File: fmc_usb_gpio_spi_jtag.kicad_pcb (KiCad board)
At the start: 4 copper layers, 76.5 x 69 mm, 146 parts, among them J1 SAMTEC_ASP-134604-01, J2 ACA-SPI-004-K02, J3 USB_C_Receptacle, J4 USB_C_Receptacle, J5 Conn_JTAG_20, J6 PM2.54-2x6, J7 Micro_SD_Card_Det2, J8 PM2.54-2x6, SW1 DSHP04TSGET, SW10 TL3342F160QG, SW2 TL3342F160QG, SW7 TL3342F160QG, SW8 TL3342F160QG, SW9 TL3342F160QG, U1 M24C02-FMN, U11 TXS02612RTWR, U12 TPD4E02B04DQA, U13 MT2492, U14 TXS02612RTWR, U15 TXS02612RTWR, U16 TXS02612RTWR, U17 TXS02612RTWR, U18 TPD4E02B04DQA, U19 TPD4E02B04DQA, U2 STUSB03EQR, U20 TPD4E02B04DQA, U21 AIP74LVC1T45GB236TR, U22 AIP74LVC1T45GB236TR, U23 AIP74LVC1T45GB236TR, U24 AIP74LVC1T45GB236TR, U25 MMC5603NJ, U26 TXS02612RTWR, U27 TXS02612RTWR, U3 CP2104, U4 TXS02612RTWR, U5 GX0011D

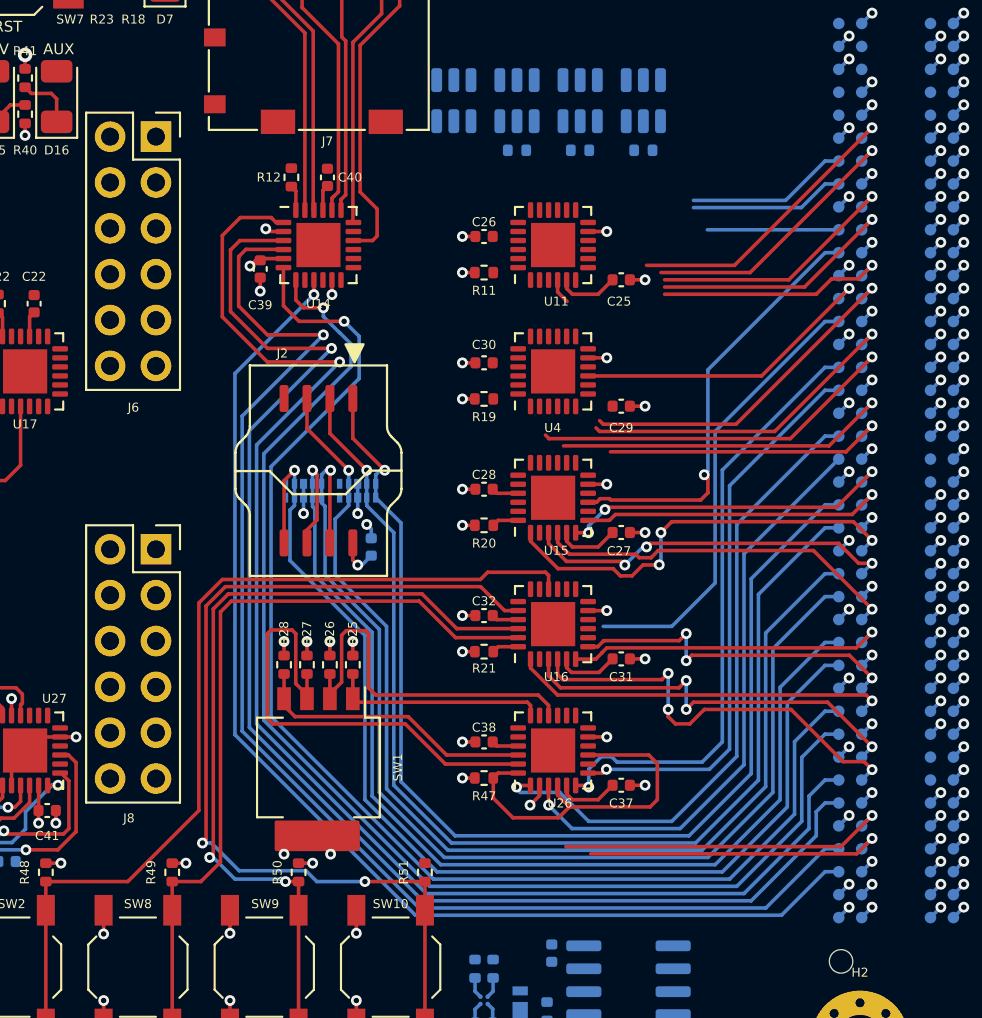
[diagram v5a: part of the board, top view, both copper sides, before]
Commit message: *.kicad_pcb: finish layout of U4, U11
Signed-off-by: Huang Rui <vowstar@gmail.com>
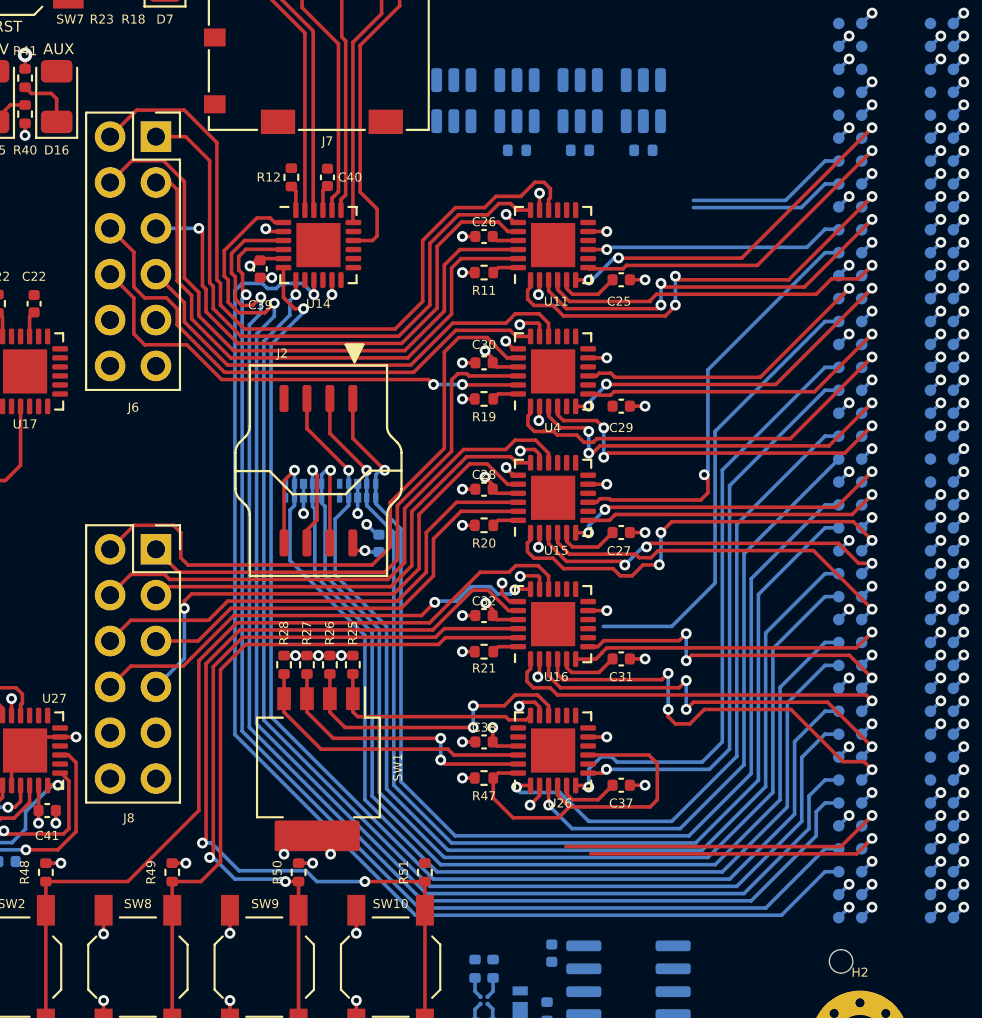
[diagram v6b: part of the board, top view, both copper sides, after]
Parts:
- moved C5 0.47 mm to (87.7, 100.5)
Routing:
- net /GPIO/HVGPIO1: track 0.00 -> 41.9 mm
- net /GPIO/HVGPIO0: track 0.00 -> 35.2 mm
- net /GPIO/HVGPIO3: track 0.00 -> 35.2 mm
- net /GPIO/HVGPIO9: track 0.00 -> 35.2 mm
- net /GPIO/HVGPIO2: track 0.00 -> 31.6 mm
- net /GPIO/HVGPIO11: track 0.00 -> 30.7 mm
- net /GPIO/HVGPIO4: track 0.00 -> 30.2 mm, vias 0 -> 1
- net /GPIO/HVGPIO5: track 0.00 -> 29.4 mm
- net /GPIO/HVGPIO8: track 0.00 -> 29.3 mm
- net /GPIO/HVGPIO14: track 0.00 -> 29.3 mm, vias 0 -> 1
- net /GPIO/HVGPIO13: track 0.00 -> 27.1 mm
- net /GPIO/HVGPIO6: track 0.00 -> 26.6 mm
- net /GPIO/HVGPIO7: track 0.00 -> 26.3 mm, vias 0 -> 2
- net /GPIO/HVGPIO15: track 0.00 -> 25.9 mm, vias 0 -> 2
- net /GPIO/HVGPIO10: track 0.00 -> 25.8 mm
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
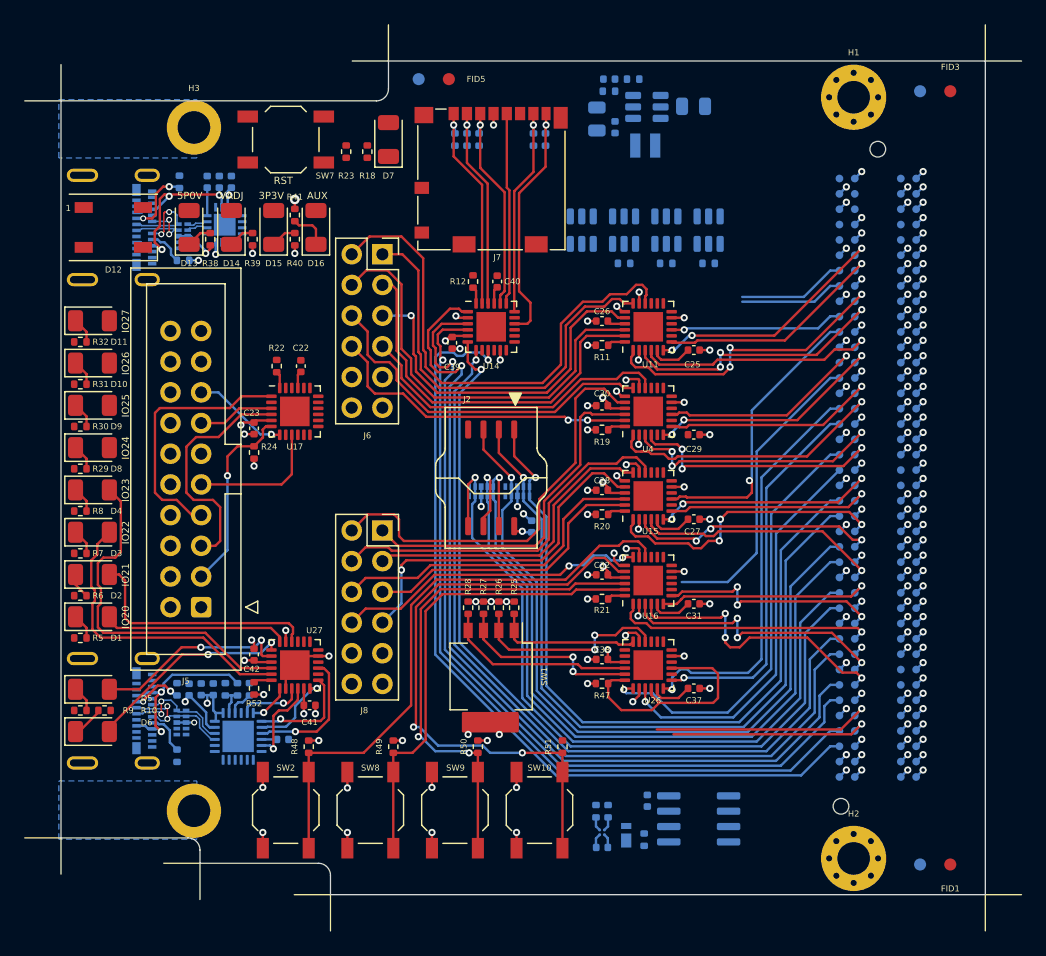
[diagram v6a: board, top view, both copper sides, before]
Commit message: *.kicad_pcb: finish 5V power layout
Signed-off-by: Huang Rui <vowstar@gmail.com>
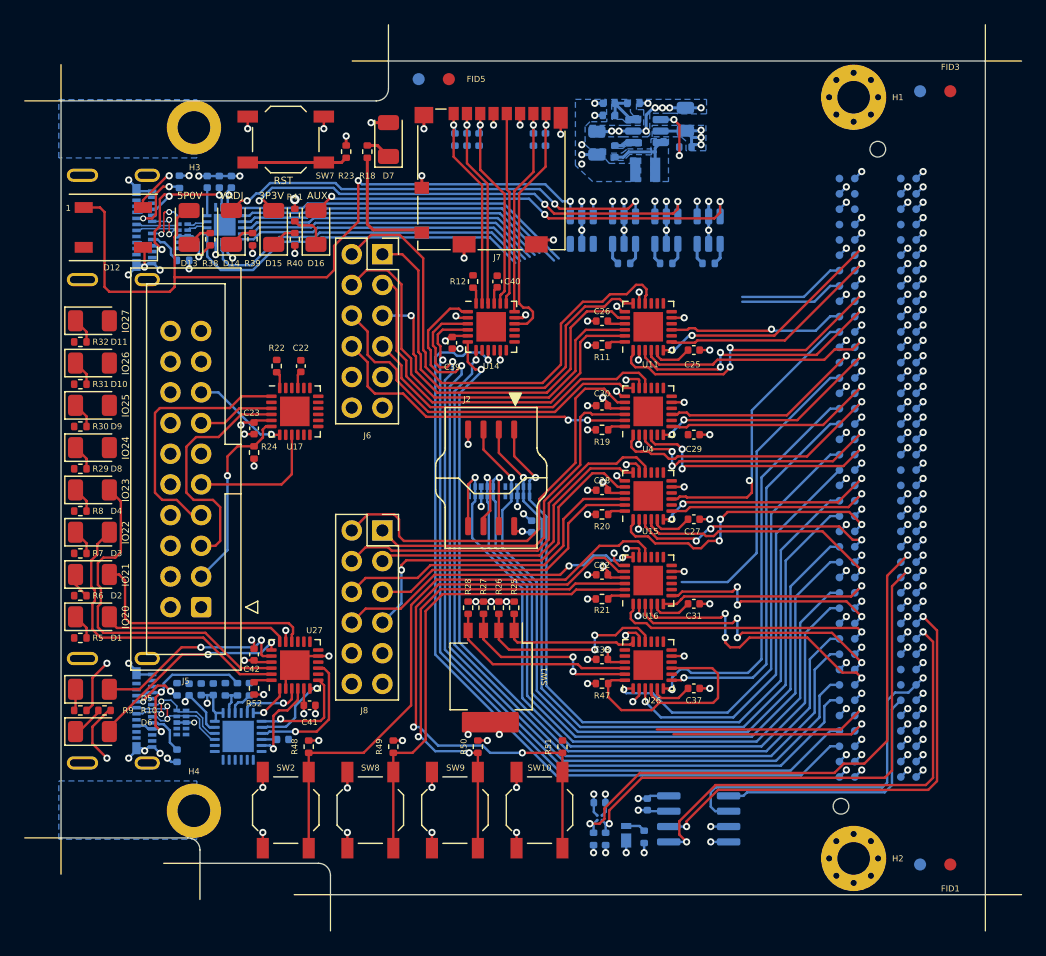
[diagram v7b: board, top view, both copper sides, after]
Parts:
- added R54: 15k, Resistor_SMD:R_0402_1005Metric, B.Cu at (100.4, 69.1)
- moved C36 3.71 mm to (93.3, 123.4), turned to 180 degrees
- moved R42 2.59 mm to (92.8, 126.4), turned to 90 degrees
- moved R43 2.43 mm to (93.8, 126.4), turned to 90 degrees
- moved R34 2.00 mm to (96.1, 65.5)
- moved C34 2.00 mm to (94.1, 65.5)
- moved C33 2.00 mm to (94.6, 69.5)
- moved C35 2.00 mm to (93.1, 68.8)
- moved L1 2.00 mm to (97.1, 71.0)
- moved R33 2.00 mm to (94.1, 66.5)
- moved U13 2.00 mm to (97.2, 67.8)
- moved C24 1.27 mm to (100.4, 66.8), turned to 90 degrees
- moved U25 1.22 mm to (93.3, 124.6), turned to -90 degrees
- moved C1 0.30 mm to (97.3, 123.5)
- moved R53 0.23 mm to (97.0, 126.2)
- turned R9 to 0 degrees
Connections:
- U13 pad 4: 12P0V -> Net-(U13-EN)
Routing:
- net GND: track 107.9 -> 180.6 mm, vias 114 -> 159
- net 5P0V: track 0.00 -> 68.8 mm, vias 0 -> 10
- net /FMC/I3C.SCL: track 1.98 -> 46.3 mm, vias 1 -> 2
- net /FMC/I3C.SDA: track 1.98 -> 45.2 mm, vias 1 -> 2
- net Net-(D15-A): track 0.00 -> 39.7 mm, vias 0 -> 3
- net /FMC/SDA: track 0.81 -> 39.1 mm, vias 1 -> 2
- net /FMC/SCL: track 0.81 -> 38.9 mm, vias 1 -> 2
- net Net-(D16-A): track 0.00 -> 37.0 mm, vias 0 -> 3
- net Net-(D14-A): track 0.00 -> 36.8 mm, vias 0 -> 3
- net /FMC/USB_FS.~{OE}: track 0.81 -> 30.6 mm
- net /FMC/USB_FS.DET: track 0.81 -> 29.8 mm
- net /FMC/USB_FS.SUS: track 0.81 -> 29.2 mm
- net /FMC/USB_FS.SPD: track 0.81 -> 28.7 mm
- net /FMC/GA0: track 0.81 -> 28.3 mm
- net /FMC/USB_FS.RCV: track 0.81 -> 27.1 mm
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- added copper zone on B.Cu, net 12P0V
- added copper zone on B.Cu, net 5P0V
- added copper zone on B.Cu, net Net-(U13-BST)
- added copper zone on B.Cu, net Net-(U13-FB)
- added copper zone on B.Cu, net Net-(U13-SW)

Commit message: *.kicad_pcb: fanout uart signals
Signed-off-by: Huang Rui <vowstar@gmail.com>
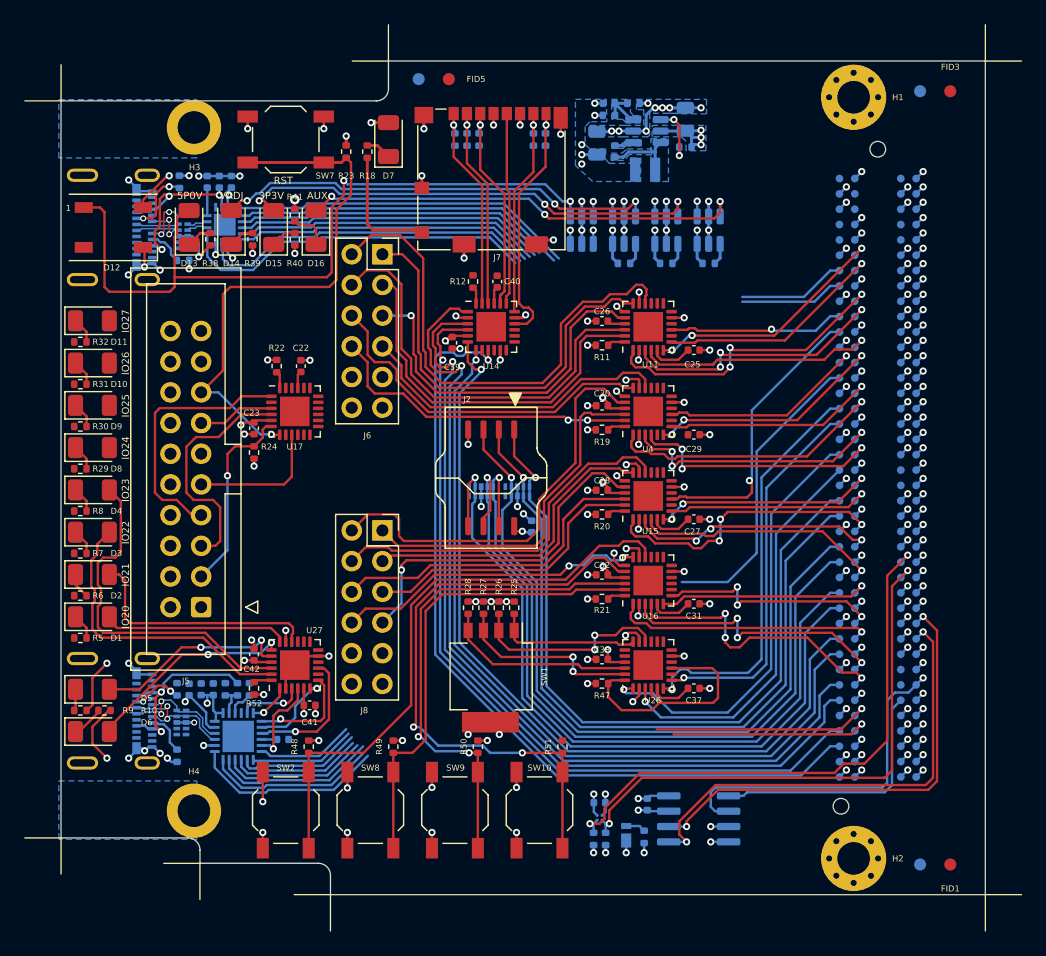
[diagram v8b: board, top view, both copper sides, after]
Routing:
- net /JTAG/~{SRST}: track 16.3 -> 45.8 mm
- net /FMC/UART.~{RI}: track 0.81 -> 16.9 mm
- net /FMC/UART.~{DCD}: track 0.81 -> 15.0 mm
- net /FMC/UART.~{DTR}: track 0.81 -> 14.4 mm
- net /FMC/UART.~{DSR}: track 0.81 -> 13.1 mm
- net /FMC/UART.TXD: track 0.81 -> 11.9 mm
- net /FMC/UART.RXD: track 0.81 -> 11.1 mm
- net /FMC/UART.~{RTS}: track 0.81 -> 9.67 mm
- net /FMC/UART.~{CTS}: track 0.81 -> 8.89 mm
- net GND: track 180.6 -> 184.2 mm, vias 159 -> 162
- net VADJ: track 36.1 -> 38.3 mm, vias 12 -> 14
- net 3P3VAUX: track 5.23 -> 6.36 mm, vias 2 -> 3
- net 3P3V: track 46.5 -> 47.6 mm, vias 28 -> 29
- net /FMC/WS2812: track 0.81 -> 1.95 mm, vias 1 -> 2
- net 5P0V: track 68.8 -> 69.5 mm
